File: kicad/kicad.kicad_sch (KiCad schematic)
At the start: 251 parts, among them sw1 Esc, sw10 Z, sw100 N5, sw101 N6, sw102 N2, sw103 N1, sw104 N0, sw105 MPlay, sw106 MFwd, sw107 NSlash, sw108 NStar, sw109 N8, sw11 LCtrl, sw110 N9, sw111 NMinus, sw112 NPlus, sw113 NEnter, sw114 N3, sw115 NPeriod, sw12 LSys, sw13 F2, sw14 F3, sw15 2, sw16 3, sw17 W, sw18 E, sw19 S, sw2 F1, sw20 D, sw21 X, sw22 C, sw23 LAlt, sw24 THome, sw25 F4, sw26 F5, sw27 4, sw28 5, sw29 R, sw3 Tilda, sw30 T, sw31 F, sw32 G, sw33 V, sw34 B, sw35 LSpace, sw36 TLeft, sw37 F6, sw38 F7, sw39 6, sw4 1, sw40 7, sw41 Y, sw42 U, sw43 H, sw44 J, sw45 N, sw46 M, sw47 TUp, sw48 TDown, sw49 F8, sw5 Tab, sw50 F9, sw51 8, sw52 9, sw53 I, sw54 O, sw55 K, sw56 L, sw57 Comma, sw58 Period, sw59 RSpace, sw6 Q, sw60 TRight, sw61 F10, sw62 F11, sw63 0, sw64 Minus, sw65 P, sw66 LBrack, sw67 Semi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

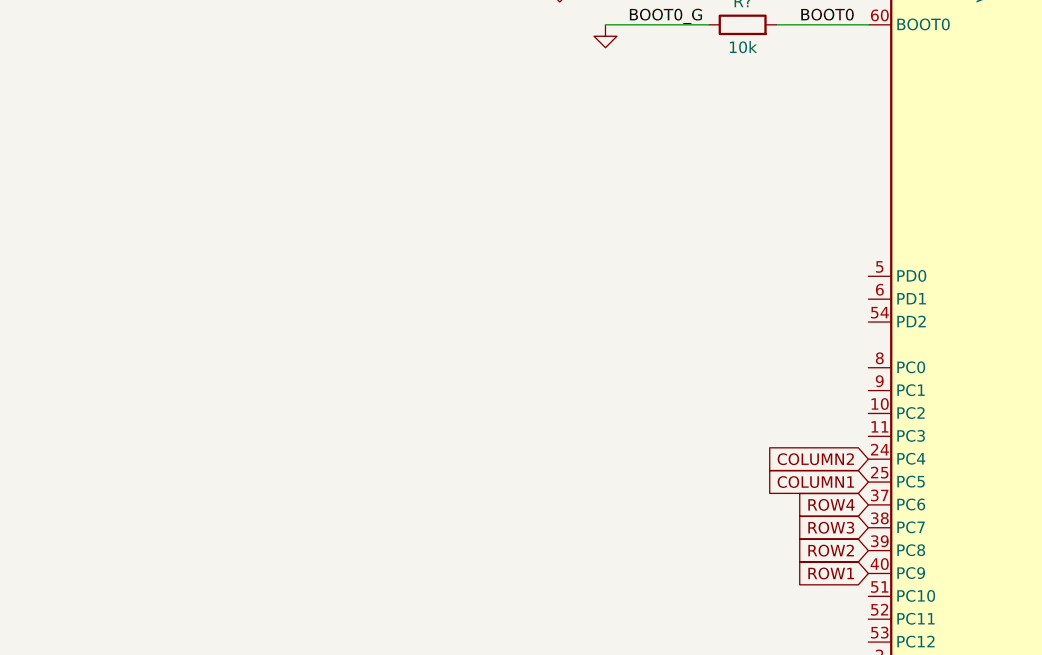
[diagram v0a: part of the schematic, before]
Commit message: finish basic oscillator circuitry
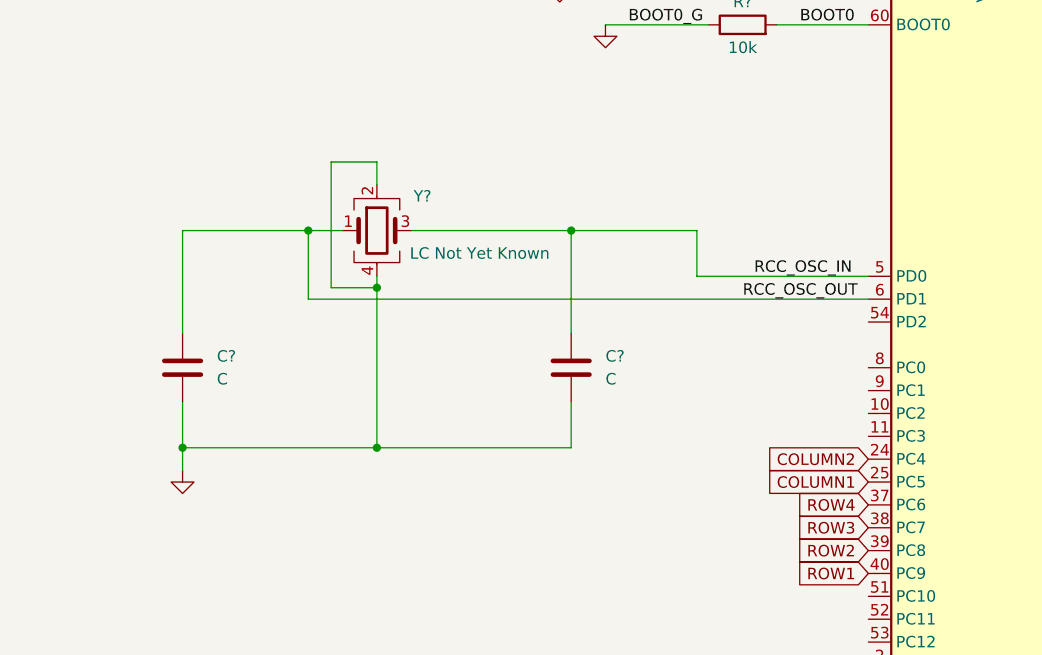
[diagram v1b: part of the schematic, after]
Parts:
- added C? (x2): C, symbol Device:C
- added Y?: LC Not Yet Known, symbol Device:Crystal_GND24
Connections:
- net GND: now also C?.2, C?.2, Y?.2, Y?.4
- net RCC_OSC_IN: now reaches MCU1.5 (PD0)
- net RCC_OSC_IN: now also C?.1, Y?.3
- net RCC_OSC_OUT: now reaches MCU1.6 (PD1)
- net RCC_OSC_OUT: now also C?.1, Y?.1

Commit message: recover small change lost in merge
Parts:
- gave numbers to parts that had none: 23
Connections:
- net COLUMN2: now also D90.2 (A)
- net COLUMN8: now also D12.2 (A)

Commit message: Passing electrical rules check
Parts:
- C1, C7: value C -> 10p
- Y1: value LC Not Yet Known -> 16MGz
- renumbered D116 to Dcaps1, D117 to Dpower1
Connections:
- net COLUMN2: now also D100.2 (A), D101.2 (A), D102.2 (A), D103.2 (A), D104.2 (A), D94.2 (A), D95.2 (A), D96.2 (A), D97.2 (A), D98.2 (A), D99.2 (A); no longer D83.2 (A), D84.2 (A), D85.2 (A), D86.2 (A), D87.2 (A), D88.2 (A), D89.2 (A), D90.2 (A), D91.2 (A), D92.2 (A), D93.2 (A)
- net COLUMN3: now also D83.2 (A), D84.2 (A), D85.2 (A), D86.2 (A), D87.2 (A), D88.2 (A), D89.2 (A), D90.2 (A), D91.2 (A), D92.2 (A), D93.2 (A); no longer D73.2 (A), D74.2 (A), D75.2 (A), D76.2 (A), D77.2 (A), D78.2 (A), D79.2 (A), D80.2 (A), D81.2 (A), D82.2 (A)
- net COLUMN4: now also D73.2 (A), D74.2 (A), D75.2 (A), D76.2 (A), D77.2 (A), D78.2 (A), D79.2 (A), D80.2 (A), D81.2 (A), D82.2 (A); no longer D61.2 (A), D62.2 (A), D63.2 (A), D64.2 (A), D65.2 (A), D66.2 (A), D67.2 (A), D68.2 (A), D69.2 (A), D70.2 (A), D71.2 (A), D72.2 (A)
- net COLUMN5: now also D61.2 (A), D62.2 (A), D63.2 (A), D64.2 (A), D65.2 (A), D66.2 (A), D67.2 (A), D68.2 (A), D69.2 (A), D70.2 (A), D71.2 (A), D72.2 (A); no longer D49.2 (A), D50.2 (A), D51.2 (A), D52.2 (A), D53.2 (A), D54.2 (A), D55.2 (A), D56.2 (A), D57.2 (A), D58.2 (A), D59.2 (A), D60.2 (A)
- net COLUMN6: now also D49.2 (A), D50.2 (A), D51.2 (A), D52.2 (A), D53.2 (A), D54.2 (A), D55.2 (A), D56.2 (A), D57.2 (A), D58.2 (A), D59.2 (A), D60.2 (A); no longer D37.2 (A), D38.2 (A), D39.2 (A), D40.2 (A), D41.2 (A), D42.2 (A), D43.2 (A), D44.2 (A), D45.2 (A), D46.2 (A), D47.2 (A), D48.2 (A)
- net COLUMN7: now also D37.2 (A), D38.2 (A), D39.2 (A), D40.2 (A), D41.2 (A), D42.2 (A), D43.2 (A), D44.2 (A), D45.2 (A), D46.2 (A), D47.2 (A), D48.2 (A); no longer D25.2 (A), D26.2 (A), D27.2 (A), D28.2 (A), D29.2 (A), D30.2 (A), D31.2 (A), D32.2 (A), D33.2 (A), D34.2 (A), D35.2 (A), D36.2 (A)
- net COLUMN8: now also D25.2 (A), D26.2 (A), D27.2 (A), D28.2 (A), D29.2 (A), D30.2 (A), D31.2 (A), D32.2 (A), D33.2 (A), D34.2 (A), D35.2 (A), D36.2 (A); no longer D1.2 (A), D10.2 (A), D11.2 (A), D12.2 (A), D2.2 (A), D3.2 (A), D4.2 (A), D5.2 (A), D6.2 (A), D7.2 (A), D8.2 (A), D9.2 (A)
- net COLUMN9: now reaches D13.2 (A), D14.2 (A), D15.2 (A), D16.2 (A), D17.2 (A), D18.2 (A), D19.2 (A), D20.2 (A), D21.2 (A), D22.2 (A), D23.2 (A), D24.2 (A)
- net COLUMN9: now also MCU1.15 (PA1)
- net COLUMN10: now reaches MCU1.14 (PA0)
- net COLUMN10: now also D1.2 (A), D10.2 (A), D11.2 (A), D12.2 (A), D2.2 (A), D3.2 (A), D4.2 (A), D5.2 (A), D6.2 (A), D7.2 (A), D8.2 (A), D9.2 (A)
- no-connect marks 0 -> 22

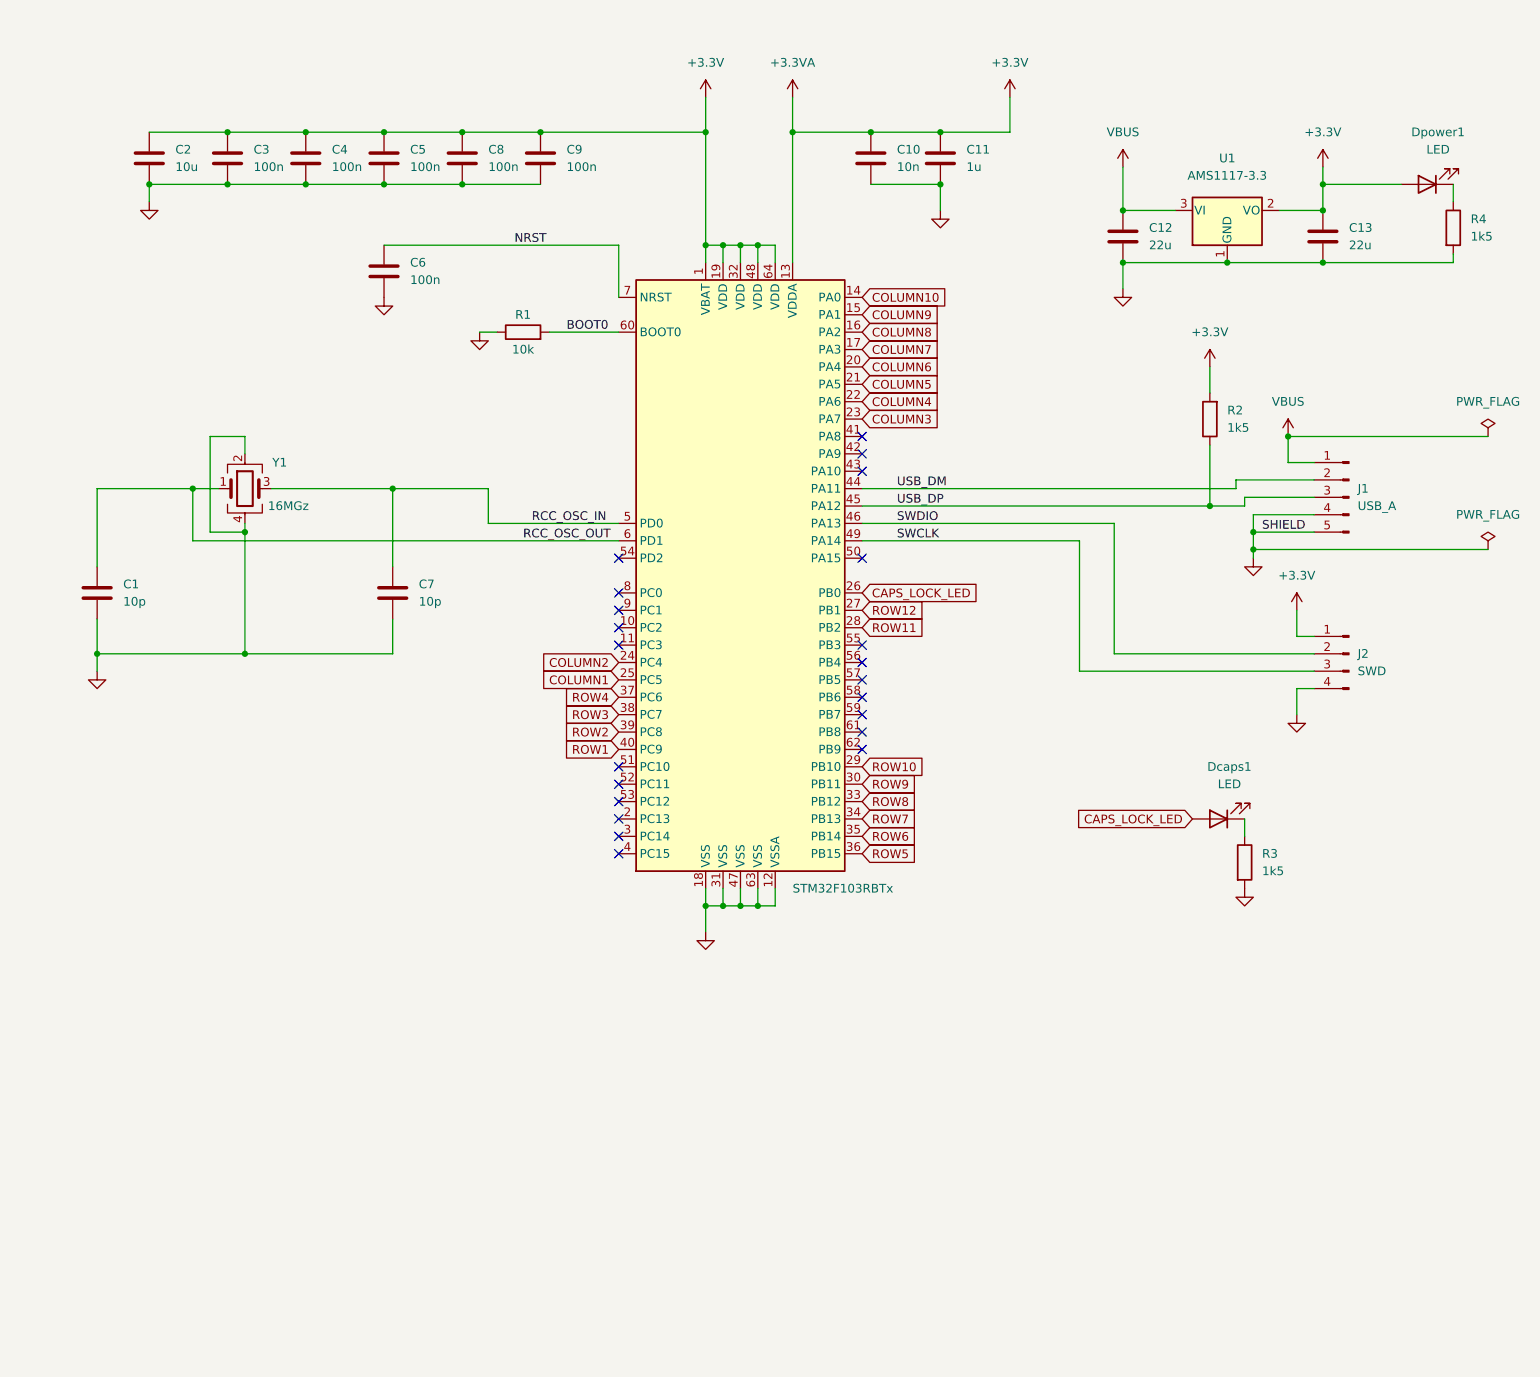
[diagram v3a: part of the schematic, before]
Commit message: Adjustments for new selected crystal part
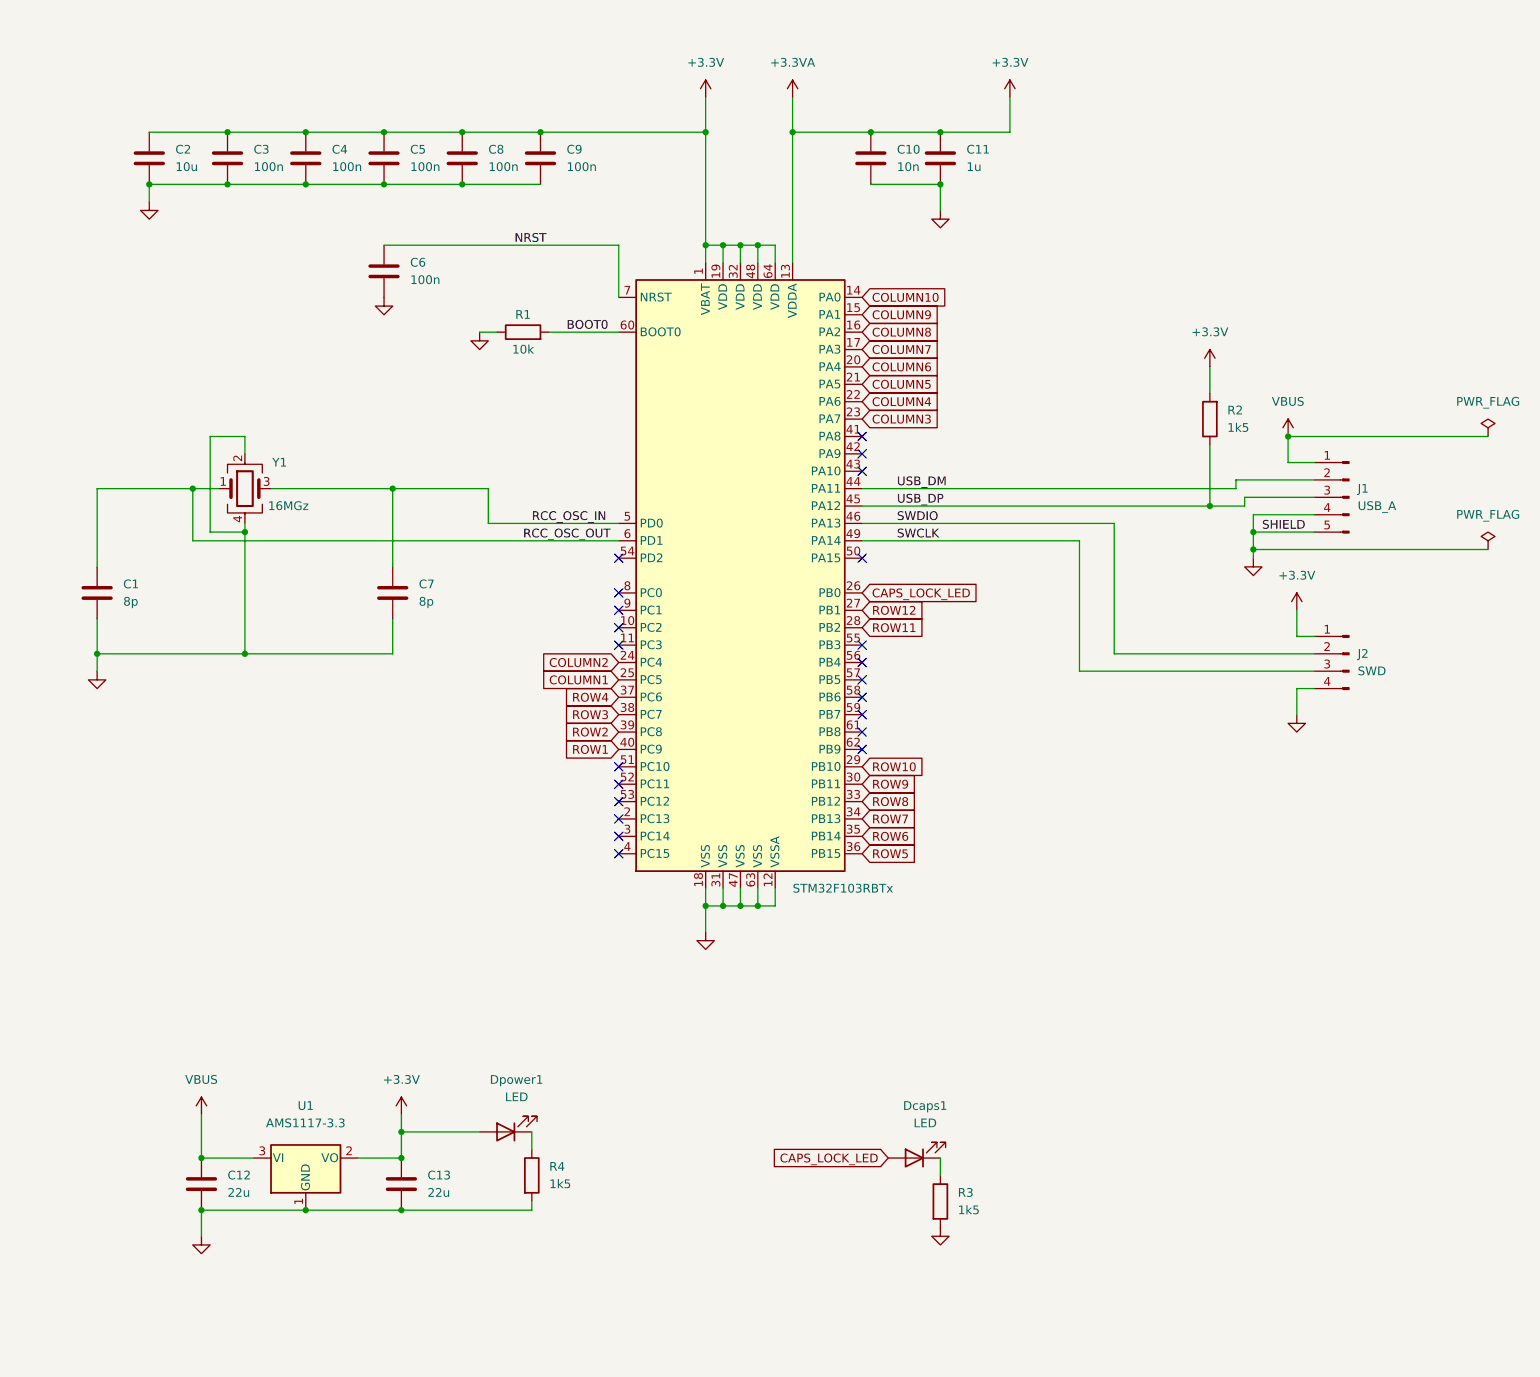
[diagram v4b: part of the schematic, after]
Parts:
- C1, C7: value 10p -> 8p
- Y1: footprint (none) -> Crystal:Crystal_SMD_3225-4Pin_3.2x2.5mm
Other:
- moved on the sheet: C12, C13, Dcaps1, Dpower1, R3, R4, U1
